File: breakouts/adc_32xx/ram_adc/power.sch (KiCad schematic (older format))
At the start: 10 parts, among them J501 Conn_01x01, J502 Conn_01x01, U501 ADM7170

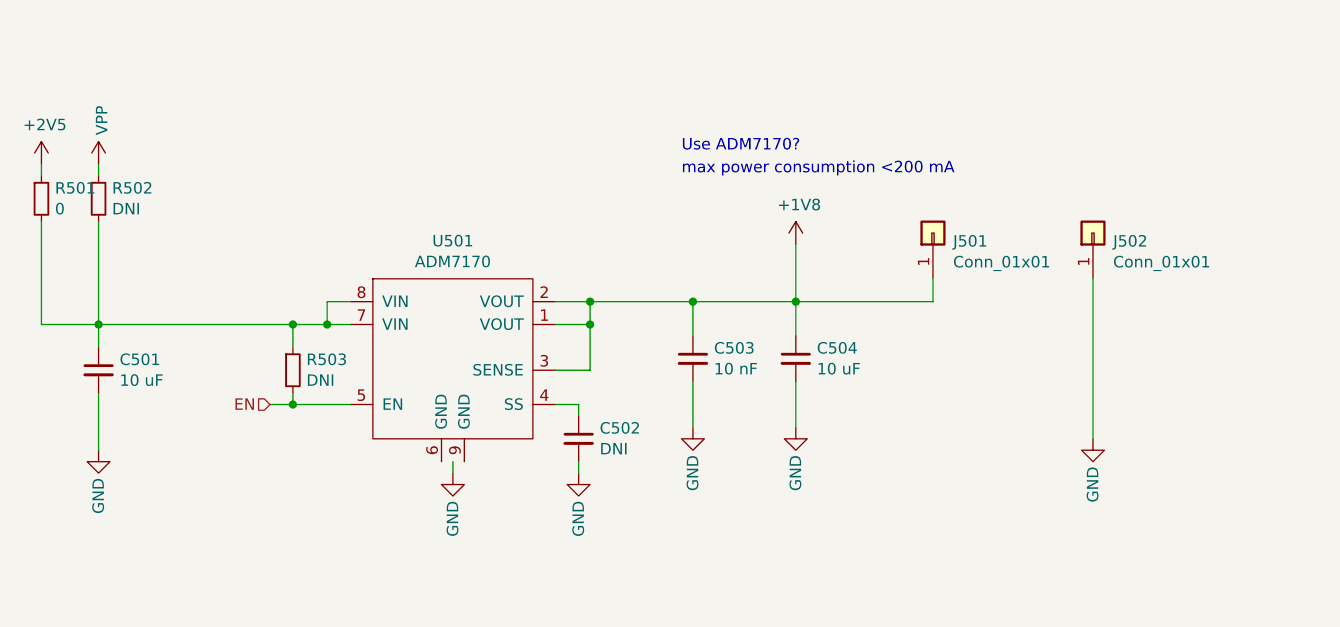
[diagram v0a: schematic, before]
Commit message: component placement for adc322x breakout
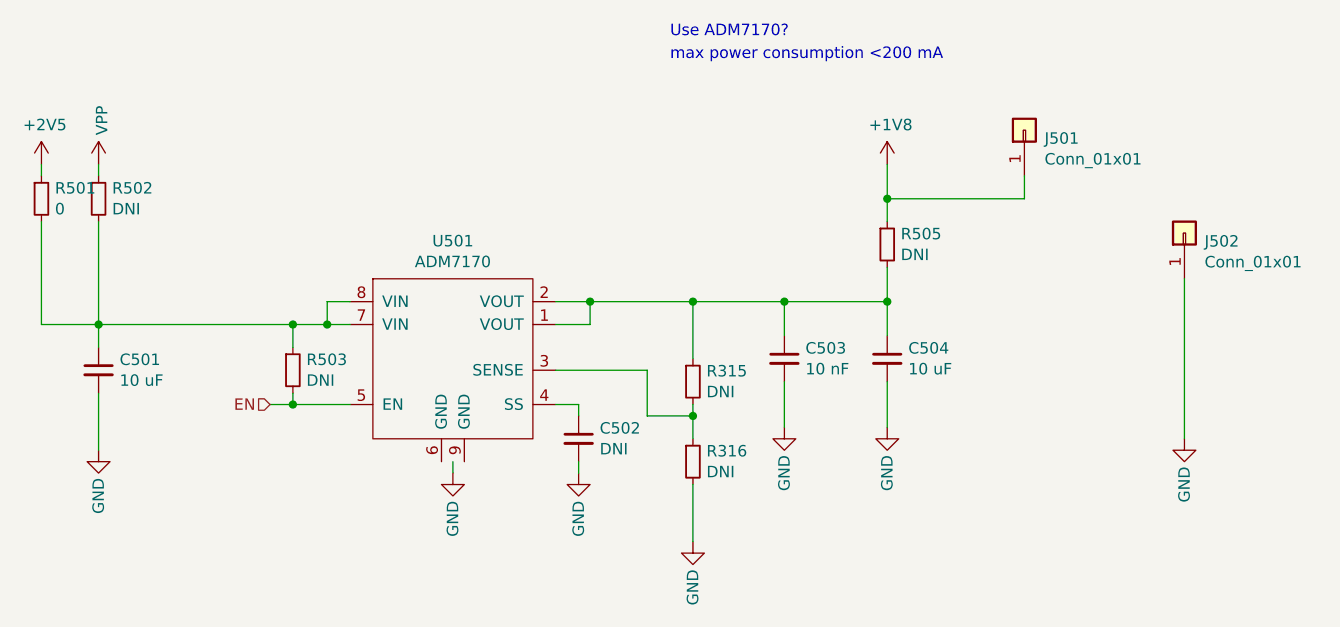
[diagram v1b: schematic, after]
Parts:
- added R315, R316, R505: DNI, Resistor_SMD:R_0402_1005Metric, symbol Device:R_Small
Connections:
- wire segments 35 -> 43
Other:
- moved on the sheet: C503, C504, J501, J502
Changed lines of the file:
@@
 $Descr A4 11693 8268
 encoding utf-8
-Sheet 5 5
+Sheet 3 5
 Title ""
 Date ""
@@
 L power:+1V8 #PWR?
 U 1 1 5ED12903
-P 5300 3200
+P 5700 2850
 AR Path="/5E9D7371/5ED12903" Ref="#PWR?"  Part="1"
 AR Path="/5ED11961/5ED12903" Ref="#PWR0506"  Part="1"
-F 0 "#PWR0506" H 5300 3050 50  0001 C CNN
-F 1 "+1V8" H 5315 3373 50  0000 C CNN
-F 2 "" H 5300 3200 50  0001 C CNN
-F 3 "" H 5300 3200 50  0001 C CNN
-	1    5300 3200
-	1    0    0    -1
-$EndComp
-Text Notes 4800 2900 0    50   ~ 0
+F 0 "#PWR0506" H 5700 2700 50  0001 C CNN
+F 1 "+1V8" H 5715 3023 50  0000 C CNN
+F 2 "" H 5700 2850 50  0001 C CNN
+F 3 "" H 5700 2850 50  0001 C CNN
+	1    5700 2850
+	1    0    0    -1
+$EndComp
+Text Notes 4750 2400 0    50   ~ 0
 max power consumption <200 mA
 Wire Wire Line
 	4250 3450 4400 3450
-Wire Wire Line
-	5300 3450 5300 3200
 Text HLabel 3000 3900 0    50   Input ~ 0
 EN
@@
 Wire Wire Line
 	4400 3550 4400 3450
-Connection ~ 4400 3550
-Connection ~ 4400 3450
 $Comp
 L Device:C_Small C503
 U 1 1 5ED1A5DC
-P 4850 3700
-F 0 "C503" H 4942 3746 50  0000 L CNN
-F 1 "10 nF" H 4942 3655 50  0000 L CNN
-F 2 "Capacitor_SMD:C_0402_1005Metric" H 4850 3700 50  0001 C CNN
-F 3 "~" H 4850 3700 50  0001 C CNN
-	1    4850 3700
+P 5250 3700
+F 0 "C503" H 5342 3746 50  0000 L CNN
+F 1 "10 nF" H 5342 3655 50  0000 L CNN
+F 2 "Capacitor_SMD:C_0402_1005Metric" H 5250 3700 50  0001 C CNN
+F 3 "~" H 5250 3700 50  0001 C CNN
+	1    5250 3700
 	1    0    0    -1
 $EndComp
@@
 L Device:C_Small C504
 U 1 1 5ED1A81F
-P 5300 3700
-F 0 "C504" H 5392 3746 50  0000 L CNN
-F 1 "10 uF" H 5392 3655 50  0000 L CNN
-F 2 "Capacitor_SMD:C_0603_1608Metric" H 5300 3700 50  0001 C CNN
-F 3 "~" H 5300 3700 50  0001 C CNN
-	1    5300 3700
+P 5700 3700
+F 0 "C504" H 5792 3746 50  0000 L CNN
+F 1 "10 uF" H 5792 3655 50  0000 L CNN
+F 2 "Capacitor_SMD:C_0603_1608Metric" H 5700 3700 50  0001 C CNN
+F 3 "~" H 5700 3700 50  0001 C CNN
+	1    5700 3700
 	1    0    0    -1
 $EndComp
@@
 L power:GND #PWR?
 U 1 1 5ED1DFE7
-P 4850 4000
+P 5250 4000
 AR Path="/5ED1DFE7" Ref="#PWR?"  Part="1"
 AR Path="/5E9D7371/5ED1DFE7" Ref="#PWR?"  Part="1"
 AR Path="/5ED11961/5ED1DFE7" Ref="#PWR0505"  Part="1"
-F 0 "#PWR0505" H 4850 3750 50  0001 C CNN
-F 1 "GND" V 4850 3800 50  0000 C CNN
-F 2 "" H 4850 4000 50  0001 C CNN
-F 3 "" H 4850 4000 50  0001 C CNN
-	1    4850 4000
+F 0 "#PWR0505" H 5250 3750 50  0001 C CNN
+F 1 "GND" V 5250 3800 50  0000 C CNN
+F 2 "" H 5250 4000 50  0001 C CNN
+F 3 "" H 5250 4000 50  0001 C CNN
+	1    5250 4000
 	1    0    0    -1
 $EndComp
@@
 L power:GND #PWR?
 U 1 1 5ED1E710
-P 5300 4000
+P 5700 4000
 AR Path="/5ED1E710" Ref="#PWR?"  Part="1"
 AR Path="/5E9D7371/5ED1E710" Ref="#PWR?"  Part="1"
 AR Path="/5ED11961/5ED1E710" Ref="#PWR0507"  Part="1"
-F 0 "#PWR0507" H 5300 3750 50  0001 C CNN
-F 1 "GND" V 5300 3800 50  0000 C CNN
-F 2 "" H 5300 4000 50  0001 C CNN
-F 3 "" H 5300 4000 50  0001 C CNN
-	1    5300 4000
-	1    0    0    -1
-$EndComp
-Wire Wire Line
-	4400 3450 4850 3450
-Wire Wire Line
-	4850 3800 4850 4000
-Wire Wire Line
-	4850 3600 4850 3450
-Connection ~ 4850 3450
-Wire Wire Line
-	4850 3450 5300 3450
-Wire Wire Line
-	5300 3600 5300 3450
-Connection ~ 5300 3450
-Wire Wire Line
-	5300 3800 5300 4000
+F 0 "#PWR0507" H 5700 3750 50  0001 C CNN
+F 1 "GND" V 5700 3800 50  0000 C CNN
+F 2 "" H 5700 4000 50  0001 C CNN
+F 3 "" H 5700 4000 50  0001 C CNN
+	1    5700 4000
+	1    0    0    -1
+$EndComp
+Wire Wire Line
+	5250 3800 5250 4000
+Wire Wire Line
+	5250 3600 5250 3450
+Connection ~ 5250 3450
+Wire Wire Line
+	5250 3450 5700 3450
+Wire Wire Line
+	5700 3600 5700 3450
+Connection ~ 5700 3450
+Wire Wire Line
+	5700 3800 5700 4000
 Wire Wire Line
 	3000 3900 3100 3900
@@
 L Connector_Generic:Conn_01x01 J501
 U 1 1 5ED2BB07
-P 5900 3150
-F 0 "J501" V 5864 3062 50  0000 R CNN
-F 1 "Conn_01x01" V 5773 3062 50  0000 R CNN
-F 2 "vna_footprints:TURRET_MILLMAX_2101" H 5900 3150 50  0001 C CNN
-F 3 "~" H 5900 3150 50  0001 C CNN
-	1    5900 3150
+P 6300 2700
+F 0 "J501" V 6264 2612 50  0000 R CNN
+F 1 "Conn_01x01" V 6173 2612 50  0000 R CNN
+F 2 "vna_footprints:TURRET_MILLMAX_2101" H 6300 2700 50  0001 C CNN
+F 3 "~" H 6300 2700 50  0001 C CNN
+	1    6300 2700
 	0    -1   -1   0
 $EndComp
@@
 L Connector_Generic:Conn_01x01 J502
 U 1 1 5ED2C0F2
-P 6600 3150
-F 0 "J502" V 6564 3062 50  0000 R CNN
-F 1 "Conn_01x01" V 6473 3062 50  0000 R CNN
-F 2 "vna_footprints:TURRET_MILLMAX_2101" H 6600 3150 50  0001 C CNN
-F 3 "~" H 6600 3150 50  0001 C CNN
-	1    6600 3150
+P 7000 3150
+F 0 "J502" V 6964 3062 50  0000 R CNN
+F 1 "Conn_01x01" V 6873 3062 50  0000 R CNN
+F 2 "vna_footprints:TURRET_MILLMAX_2101" H 7000 3150 50  0001 C CNN
+F 3 "~" H 7000 3150 50  0001 C CNN
+	1    7000 3150
 	0    -1   -1   0
 $EndComp
@@
 L power:GND #PWR?
 U 1 1 5ED2C38D
-P 6600 4050
+P 7000 4050
 AR Path="/5ED2C38D" Ref="#PWR?"  Part="1"
 AR Path="/5E9D7371/5ED2C38D" Ref="#PWR?"  Part="1"
 AR Path="/5ED11961/5ED2C38D" Ref="#PWR0508"  Part="1"
-F 0 "#PWR0508" H 6600 3800 50  0001 C CNN
-F 1 "GND" V 6600 3850 50  0000 C CNN
-F 2 "" H 6600 4050 50  0001 C CNN
-F 3 "" H 6600 4050 50  0001 C CNN
-	1    6600 4050
-	1    0    0    -1
-$EndComp
-Wire Wire Line
-	6600 3350 6600 4050
-Wire Wire Line
-	5300 3450 5900 3450
-Wire Wire Line
-	5900 3450 5900 3350
-Text Notes 4800 2800 0    50   ~ 0
+F 0 "#PWR0508" H 7000 3800 50  0001 C CNN
+F 1 "GND" V 7000 3850 50  0000 C CNN
+F 2 "" H 7000 4050 50  0001 C CNN
+F 3 "" H 7000 4050 50  0001 C CNN
+	1    7000 4050
+	1    0    0    -1
+$EndComp
+Wire Wire Line
+	7000 3350 7000 4050
+Text Notes 4750 2300 0    50   ~ 0
 Use ADM7170?
 Wire Wire Line
@@
 Wire Wire Line
 	4350 4150 4350 4200
-Wire Wire Line
-	4250 3750 4400 3750
-Wire Wire Line
-	4400 3550 4400 3750
+$Comp
+L Device:R_Small R505
+U 1 1 5EB8A70D
+P 5700 3200
+F 0 "R505" H 5759 3246 50  0000 L CNN
+F 1 "DNI" H 5759 3155 50  0000 L CNN
+F 2 "Resistor_SMD:R_0402_1005Metric" H 5700 3200 50  0001 C CNN
+F 3 "~" H 5700 3200 50  0001 C CNN
+	1    5700 3200
+	1    0    0    -1
+$EndComp
+Wire Wire Line
+	5700 3300 5700 3450
+Wire Wire Line
+	5700 3100 5700 3000
+Wire Wire Line
+	6300 2900 6300 3000
+Wire Wire Line
+	6300 3000 5700 3000
+Connection ~ 5700 3000
+Wire Wire Line
+	5700 3000 5700 2850
+$Comp
+L Device:R_Small R315
+U 1 1 5EBF1035
+P 4850 3800
+F 0 "R315" H 4909 3846 50  0000 L CNN
+F 1 "DNI" H 4909 3755 50  0000 L CNN
+F 2 "Resistor_SMD:R_0402_1005Metric" H 4850 3800 50  0001 C CNN
+F 3 "~" H 4850 3800 50  0001 C CNN
+	1    4850 3800
+	1    0    0    -1
+$EndComp
+$Comp
+L Device:R_Small R316
+U 1 1 5EBF1F67
+P 4850 4150
+F 0 "R316" H 4909 4196 50  0000 L CNN
+F 1 "DNI" H 4909 4105 50  0000 L CNN
+F 2 "Resistor_SMD:R_0402_1005Metric" H 4850 4150 50  0001 C CNN
+F 3 "~" H 4850 4150 50  0001 C CNN
+	1    4850 4150
+	1    0    0    -1
+$EndComp
+Wire Wire Line
+	4850 3900 4850 3950
+Wire Wire Line
+	4400 3450 4850 3450
+Connection ~ 4400 3450
+$Comp
+L power:GND #PWR?
+U 1 1 5EBFA973
+P 4850 4500
+AR Path="/5EBFA973" Ref="#PWR?"  Part="1"
+AR Path="/5E9D7371/5EBFA973" Ref="#PWR?"  Part="1"
+AR Path="/5ED11961/5EBFA973" Ref="#PWR0104"  Part="1"
+F 0 "#PWR0104" H 4850 4250 50  0001 C CNN
+F 1 "GND" V 4850 4300 50  0000 C CNN
+F 2 "" H 4850 4500 50  0001 C CNN
+F 3 "" H 4850 4500 50  0001 C CNN
+	1    4850 4500
+	1    0    0    -1
+$EndComp
+Wire Wire Line
+	4850 4250 4850 4500
+Wire Wire Line
+	4650 3750 4650 3950
+Wire Wire Line
+	4650 3950 4850 3950
+Wire Wire Line
+	4250 3750 4650 3750
+Connection ~ 4850 3950
+Wire Wire Line
+	4850 3950 4850 4050
+Wire Wire Line
+	4850 3450 4850 3700
+Connection ~ 4850 3450
+Wire Wire Line
+	4850 3450 5250 3450
 $EndSCHEMATC

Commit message: finished layout of adc32xx ecp5 board
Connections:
- net GND: now also U501.6 (GND), U501.9 (GND)
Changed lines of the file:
@@
 L power:GND #PWR?
 U 1 1 5ED1D65E
-P 3800 4200
+P 3800 4250
 AR Path="/5ED1D65E" Ref="#PWR?"  Part="1"
 AR Path="/5E9D7371/5ED1D65E" Ref="#PWR?"  Part="1"
 AR Path="/5ED11961/5ED1D65E" Ref="#PWR0504"  Part="1"
-F 0 "#PWR0504" H 3800 3950 50  0001 C CNN
-F 1 "GND" V 3800 4000 50  0000 C CNN
-F 2 "" H 3800 4200 50  0001 C CNN
-F 3 "" H 3800 4200 50  0001 C CNN
-	1    3800 4200
-	1    0    0    -1
-$EndComp
-Wire Wire Line
-	3800 4150 3800 4200
+F 0 "#PWR0504" H 3800 4000 50  0001 C CNN
+F 1 "GND" V 3800 4050 50  0000 C CNN
+F 2 "" H 3800 4250 50  0001 C CNN
+F 3 "" H 3800 4250 50  0001 C CNN
+	1    3800 4250
+	1    0    0    -1
+$EndComp
+Wire Wire Line
+	3800 4200 3800 4250
 $Comp
 L power:GND #PWR?
@@
 Wire Wire Line
 	4850 3450 5250 3450
+Wire Wire Line
+	3750 4150 3750 4200
+Wire Wire Line
+	3750 4200 3800 4200
+Wire Wire Line
+	3800 4200 3850 4200
+Wire Wire Line
+	3850 4200 3850 4150
+Connection ~ 3800 4200
 $EndSCHEMATC

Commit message: writing to wishbone from the fpga works..
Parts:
- U501: symbol vna_mm:ADM7170 -> adc_32xx-rescue:ADM7170-vna_mm
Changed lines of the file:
@@
 	3250 3550 3350 3550
 $Comp
-L vna_mm:ADM7170 U501
+L adc_32xx-rescue:ADM7170-vna_mm U501
 U 1 1 5E9F6CDD
 P 3800 3600
